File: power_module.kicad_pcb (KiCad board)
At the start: 4 copper layers, 95 x 66 mm, 71 parts, among them J1 USB_C_PD, J2 OUTPUT, J3 I2C_BREAKOUT, Q1 DUAL_N_FET, Q2 DUAL_N_FET, Q3 DUAL_N_FET, Q4 DUAL_N_FET, SW1 ON_OFF, U1 BQ7692003, U2 CH224K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

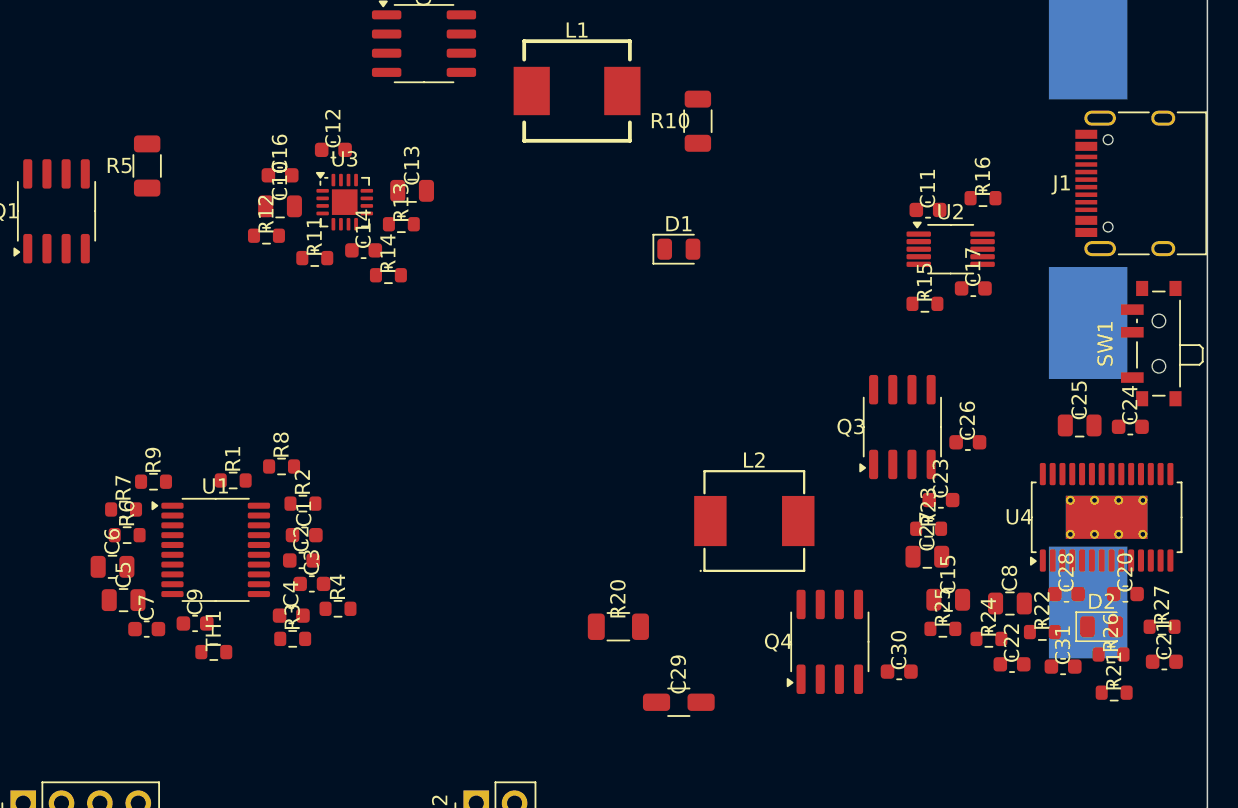
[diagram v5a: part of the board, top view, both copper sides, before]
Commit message: pcb: relax_placement pass (ICs locked, satellites moved)
Used the new relax_placement tool (KiCAD-MCP-Server develop bd9569e)
with all major ICs / FETs / inductors / LEDs locked, allowing only
caps + resistors to move. 200 iters, default spring/repulsion params.

Result vs pre-relax:
  - Ratsnest length: 1369 mm → 1216 mm (-11%)
  - Ratsnest crossings (v1 metric, component-center): 60 → 51 (-15%)
  - 54 components moved (top mover R3 by 18 mm)
  - 0 pad-copper-overlap errors, 21 tiny courtyard touches
    (max 0.88 mm², all < 1 mm² — acceptable for routing)

C8 needed a manual place_near nudge afterward (the relax v1's bbox
repulsion didn't fully resolve its 0.022 mm² pad-touch with U4 — see
tasks #185 + #178). place_near with clearanceMargin=0.5 mm found
(79.26, 50.95) which clears U4 properly.

Top remaining congestion regions are inherently dense (U4 buck-boost
fan-out, U1 BMS bypass cluster) — not a placement problem but a
"3D-stacking would help" problem we can't solve in 2D.
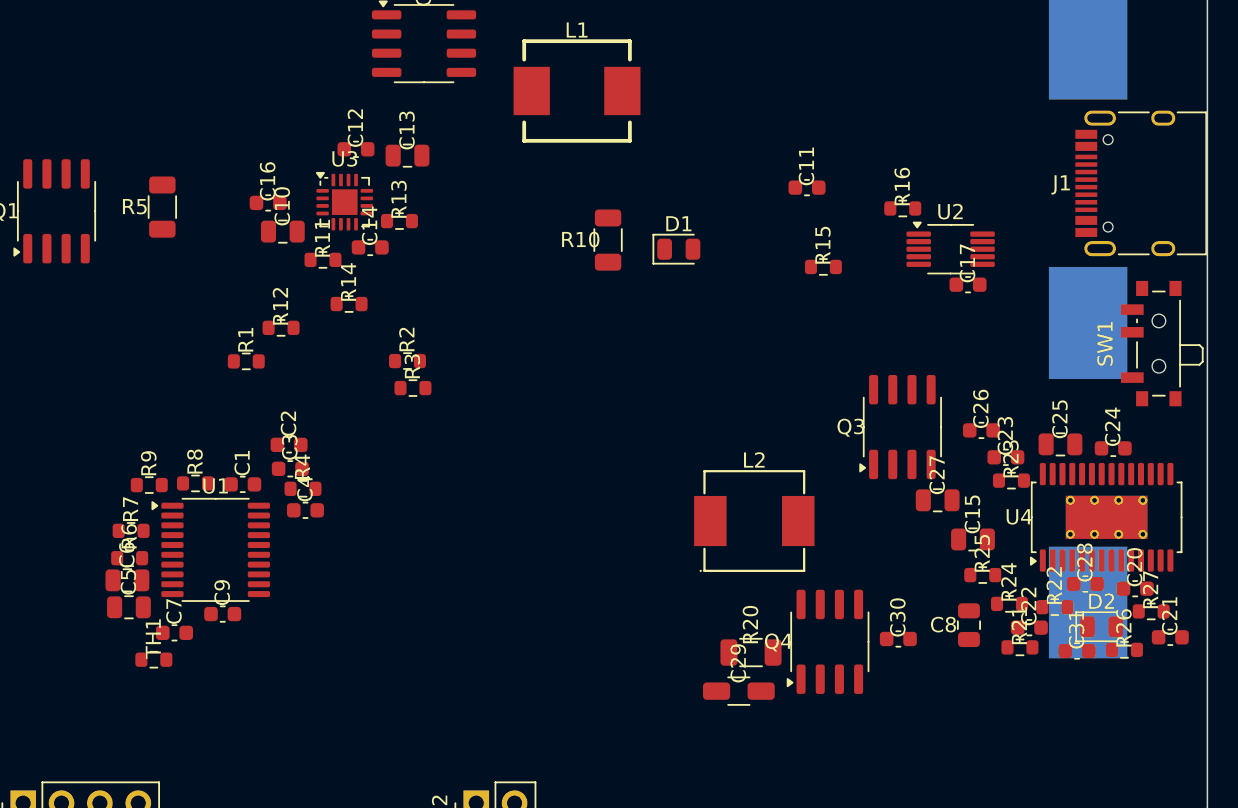
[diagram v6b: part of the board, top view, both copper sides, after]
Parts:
- moved R3 18.4 mm to (42.4, 35.3)
- moved R2 11.7 mm to (42.1, 33.5)
- moved R10 9.87 mm to (55.4, 25.5)
- moved R20 8.95 mm to (64.8, 52.8)
- moved R4 8.28 mm to (35.2, 41.9)
- moved C11 8.15 mm to (68.5, 22.0)
- moved R1 7.93 mm to (31.4, 33.5)
- moved C3 7.75 mm to (34.3, 40.6)
- moved C2 7.70 mm to (34.2, 39.0)
- moved R15 7.15 mm to (69.6, 27.2)
- moved C4 7.04 mm to (35.3, 43.3)
- moved R21 6.92 mm to (82.6, 52.4)
- moved R23 6.35 mm to (82.1, 41.4)
- moved R12 6.18 mm to (33.7, 31.3)
- moved R8 5.81 mm to (28.0, 41.6)
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
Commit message: Locked U4
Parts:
- moved SW1 0.53 mm to (91.5, 31.8)
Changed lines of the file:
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@@
 	(footprint "Button_Switch_SMD:SW_SPDT_PCM12"
 		(layer "F.Cu")
-		(at 91.509276 32.308559 90)
+		(at 91.509276 31.774 90)
 		(descr "Ultraminiature Surface Mount Slide Switch, right-angle, https://www.ckswitches.com/media/1424/pcm.pdf")
 		(property "Reference" "SW1"
@@
 	)
 	(footprint "Package_SO:HTSSOP-28-1EP_4.4x9.7mm_P0.65mm_EP2.85x5.4mm_ThermalVias"
+		(locked yes)
 		(layer "F.Cu")
 		(at 88.377946 43.812013 90)
